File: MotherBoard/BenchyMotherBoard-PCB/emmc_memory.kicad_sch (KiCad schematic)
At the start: 82 parts, among them J24 Micro_SD_Card_Det1, J25 Micro_SD_Card_Det1, U34 74HCT2G08, U4 AM6254ATCGGAALW, U52 IS21ES08GA-JCLI, U53 S28HS512TGABHI010, U54 SIP32510DT-T1-GE3, U55 SIP32510DT-T1-GE3, U56 IP4252CZ16-8-TTL, U57 IP4252CZ16-8-TTL, U59 74HCT2G08, U60 74HCT2G08

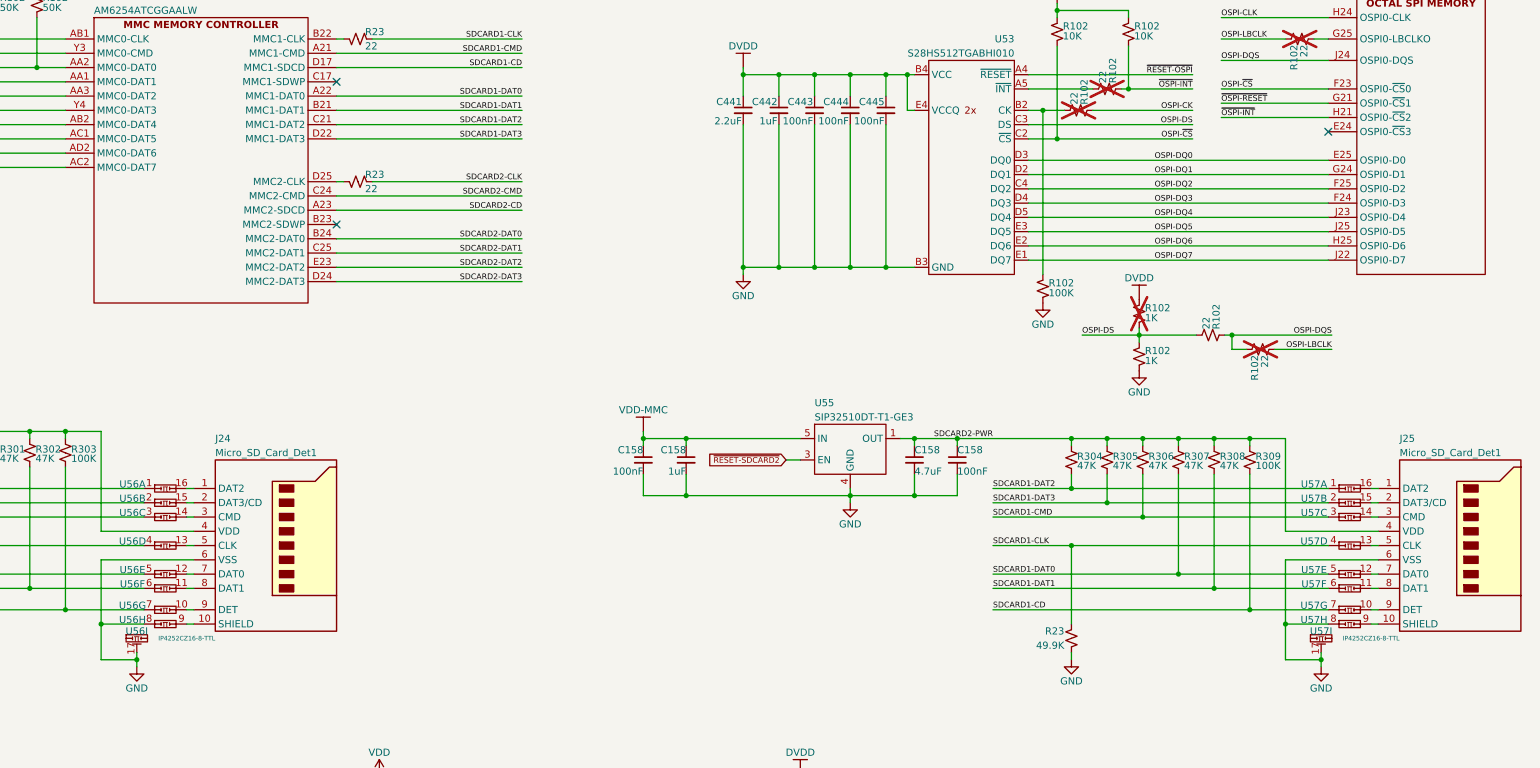
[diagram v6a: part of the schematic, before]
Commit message: Add docs for benchy reloaded
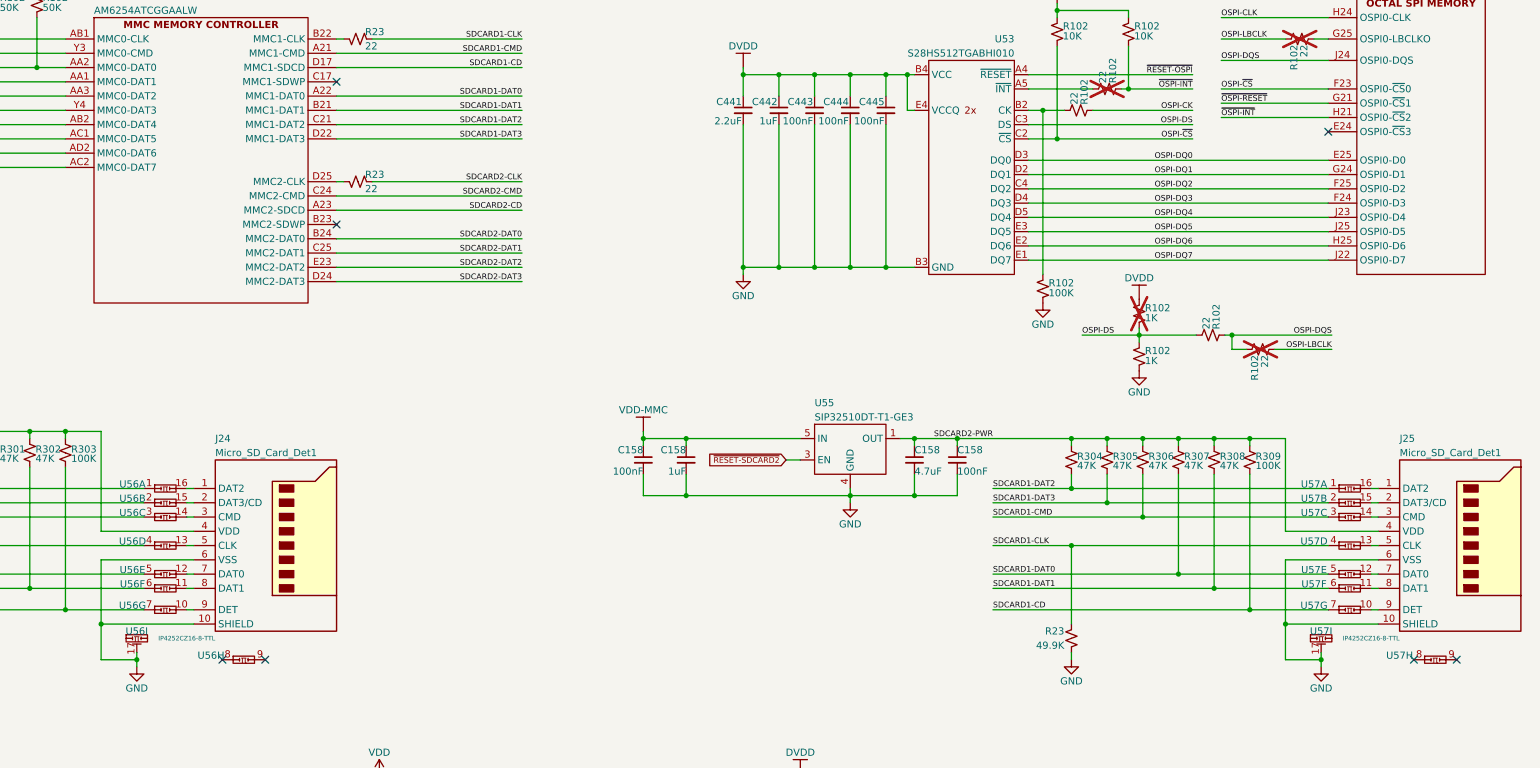
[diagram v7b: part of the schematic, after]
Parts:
- R102: now fitted
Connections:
- net GND: now also J24.10 (SHIELD), J25.10 (SHIELD); no longer U56.8 (8A), U57.8 (8A)
- net at U56.9 (8B): no longer J24.10 (SHIELD)
- net at U57.9 (8B): no longer J25.10 (SHIELD)
- no-connect marks 3 -> 7
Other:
- moved on the sheet: U56H, U57H
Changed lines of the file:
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@@
   (junction (at 59.69 190.5) (diameter 0) (color 0 0 0 0)
   )
+  (junction (at 370.84 134.62) (diameter 0) (color 0 0 0 0)
+  )
   (junction (at 153.67 132.08) (diameter 0) (color 0 0 0 0)
   )
@@
   (junction (at 264.16 101.6) (diameter 0) (color 0 0 0 0)
   )
-  (junction (at 160.02 134.62) (diameter 0) (color 0 0 0 0)
-  )
   (junction (at 93.98 22.86) (diameter 0) (color 0 0 0 0)
   )
@@
   (junction (at 132.08 162.56) (diameter 0) (color 0 0 0 0)
   )
-  (junction (at 370.84 134.62) (diameter 0) (color 0 0 0 0)
-  )
   (junction (at 127 62.23) (diameter 0) (color 0 0 0 0)
   )
@@
   (junction (at 59.69 163.83) (diameter 0) (color 0 0 0 0)
   )
+  (junction (at 160.02 134.62) (diameter 0) (color 0 0 0 0)
+  )
   (junction (at 280.67 162.56) (diameter 0) (color 0 0 0 0)
   )
@@
   (no_connect (at 201.93 63.5))
   (no_connect (at 201.93 38.1))
+  (no_connect (at 401.32 140.97))
+  (no_connect (at 181.61 140.97))
+  (no_connect (at 189.23 140.97))
+  (no_connect (at 393.7 140.97))
   (wire (pts (xy 351.79 107.95) (xy 351.79 125.73))
     (stroke (width 0) (type default))
@@
     (stroke (width 0) (type default))
   )
-  (wire (pts (xy 370.84 134.62) (xy 370.84 140.97))
+  (wire (pts (xy 370.84 123.19) (xy 370.84 134.62))
     (stroke (width 0) (type default))
   )
@@
     (stroke (width 0) (type default))
   )
+  (wire (pts (xy 370.84 134.62) (xy 387.35 134.62))
+    (stroke (width 0) (type default))
+  )
   (wire (pts (xy 280.67 45.72) (xy 280.67 71.12))
     (stroke (width 0) (type default))
@@
     (stroke (width 0) (type default))
   )
+  (wire (pts (xy 370.84 134.62) (xy 370.84 140.97))
+    (stroke (width 0) (type default))
+  )
   (wire (pts (xy 74.93 22.86) (xy 74.93 30.48))
     (stroke (width 0) (type default))
@@
     (stroke (width 0) (type default))
   )
+  (wire (pts (xy 160.02 134.62) (xy 160.02 140.97))
+    (stroke (width 0) (type default))
+  )
   (wire (pts (xy 312.42 111.76) (xy 304.8 111.76))
     (stroke (width 0) (type default))
@@
     (stroke (width 0) (type default))
   )
-  (wire (pts (xy 160.02 134.62) (xy 167.64 134.62))
-    (stroke (width 0) (type default))
-  )
   (wire (pts (xy 336.55 43.18) (xy 354.33 43.18))
     (stroke (width 0) (type default))
@@
     (stroke (width 0) (type default))
   )
-  (wire (pts (xy 175.26 134.62) (xy 176.53 134.62))
-    (stroke (width 0) (type default))
-  )
   (wire (pts (xy 378.46 110.49) (xy 332.74 110.49))
     (stroke (width 0) (type default))
@@
     (stroke (width 0) (type default))
   )
-  (wire (pts (xy 370.84 123.19) (xy 370.84 134.62))
-    (stroke (width 0) (type default))
-  )
   (wire (pts (xy 160.02 100.33) (xy 160.02 118.11))
     (stroke (width 0) (type default))
@@
     (stroke (width 0) (type default))
   )
-  (wire (pts (xy 160.02 134.62) (xy 160.02 140.97))
-    (stroke (width 0) (type default))
-  )
   (wire (pts (xy 293.37 71.12) (xy 299.72 71.12))
     (stroke (width 0) (type default))
@@
     (stroke (width 0) (type default))
   )
+  (wire (pts (xy 160.02 134.62) (xy 176.53 134.62))
+    (stroke (width 0) (type default))
+  )
   (wire (pts (xy 304.8 107.95) (xy 304.8 111.76))
     (stroke (width 0) (type default))
@@
     (stroke (width 0) (type default))
   )
-  (wire (pts (xy 370.84 134.62) (xy 378.46 134.62))
-    (stroke (width 0) (type default))
-  )
   (wire (pts (xy 59.69 191.77) (xy 59.69 190.5))
     (stroke (width 0) (type default))
@@
     (stroke (width 0) (type default))
   )
-  (wire (pts (xy 386.08 134.62) (xy 387.35 134.62))
-    (stroke (width 0) (type default))
-  )
   (wire (pts (xy 153.67 100.33) (xy 153.67 101.6))
     (stroke (width 0) (type default))
@@
     )
   )
-  (symbol (lib_id "Daxxn_Protection:IP4252CZ16-8-TTL") (at 171.45 134.62 0) (unit 8)
+  (symbol (lib_id "Daxxn_Protection:IP4252CZ16-8-TTL") (at 185.42 140.97 0) (unit 8)
     (in_bom yes) (on_board yes) (dnp no)
-    (property "Reference" "U56" (at 165.608 133.858 0)
+    (property "Reference" "U56" (at 179.578 140.208 0)
       (effects (font (size 1.27 1.27)))
     )
-    (property "Value" "IP4252CZ16-8-TTL" (at 171.45 131.826 0)
+    (property "Value" "IP4252CZ16-8-TTL" (at 185.42 138.176 0)
       (effects (font (size 0.8 0.8)) hide)
     )
-    (property "Footprint" "Daxxn_Packages:QFN16_SOT1168-1_NEX-M" (at 171.45 128.27 0)
+    (property "Footprint" "Daxxn_Packages:QFN16_SOT1168-1_NEX-M" (at 185.42 134.62 0)
       (effects (font (size 1.27 1.27)) hide)
     )
-    (property "Datasheet" "%LOCAL_DATASHEETS%/IP4251-TTL.pdf" (at 171.45 125.73 0)
+    (property "Datasheet" "%LOCAL_DATASHEETS%/IP4251-TTL.pdf" (at 185.42 132.08 0)
       (effects (font (size 1.27 1.27)) hide)
     )
@@
     )
   )
-  (symbol (lib_id "Daxxn_Protection:IP4252CZ16-8-TTL") (at 382.27 134.62 0) (unit 8)
+  (symbol (lib_id "Daxxn_Protection:IP4252CZ16-8-TTL") (at 397.51 140.97 0) (unit 8)
     (in_bom yes) (on_board yes) (dnp no)
-    (property "Reference" "U57" (at 375.92 133.858 0)
+    (property "Reference" "U57" (at 391.16 140.208 0)
       (effects (font (size 1.27 1.27)))
     )
-    (property "Value" "IP4252CZ16-8-TTL" (at 421.132 134.62 0)
+    (property "Value" "IP4252CZ16-8-TTL" (at 436.372 140.97 0)
       (effects (font (size 0.8 0.8)) hide)
     )
-    (property "Footprint" "Daxxn_Packages:QFN16_SOT1168-1_NEX-M" (at 382.27 128.27 0)
+    (property "Footprint" "Daxxn_Packages:QFN16_SOT1168-1_NEX-M" (at 397.51 134.62 0)
       (effects (font (size 1.27 1.27)) hide)
     )
-    (property "Datasheet" "%LOCAL_DATASHEETS%/IP4251-TTL.pdf" (at 382.27 125.73 0)
+    (property "Datasheet" "%LOCAL_DATASHEETS%/IP4251-TTL.pdf" (at 397.51 132.08 0)
       (effects (font (size 1.27 1.27)) hide)
     )
@@
   )
   (symbol (lib_id "Daxxn_Device:R") (at 334.01 43.18 90) (unit 1)
-    (in_bom yes) (on_board yes) (dnp yes)
+    (in_bom yes) (on_board yes) (dnp no)
     (property "Reference" "R102" (at 335.026 42.164 0)
       (effects (font (size 1.27 1.27)) (justify left))

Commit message: Replacing motherboard and more - SAVE
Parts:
- renumbered C158 to C447, C158 to C448, C158 to C449, C158 to C450, C158 to C451, C158 to C452, C158 to C453, C158 to C454, C158 to C455, C158 to C456, C158 to C457, C158 to C458, R102 to R281, R102 to R282, R23 to R283, R102 to R284, R102 to R285, R23 to R286, R102 to R287, R102 to R288, R102 to R289, R23 to R290, R23 to R291, R102 to R292, R102 to R293, R102 to R294, R102 to R295, R102 to R296, R102 to R297, R23 to R310, R23 to R311, R102 to R312, R102 to R313, R102 to R314, R102 to R315, R102 to R316, R102 to R317, R102 to R318, R102 to R319, R102 to R320, U4 to U1, U34 to U58, U34 to U61
